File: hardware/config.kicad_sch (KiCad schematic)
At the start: 40 parts, among them J4 JTAG, SW1 219-2MST, U4 GateMate-CCGM1A1, U6 74LVC1G04GM,115, U7 74LVC2G00HK3-7, U8 74LVC2G00HK3-7, U9 AT25QL321-MBUE-T

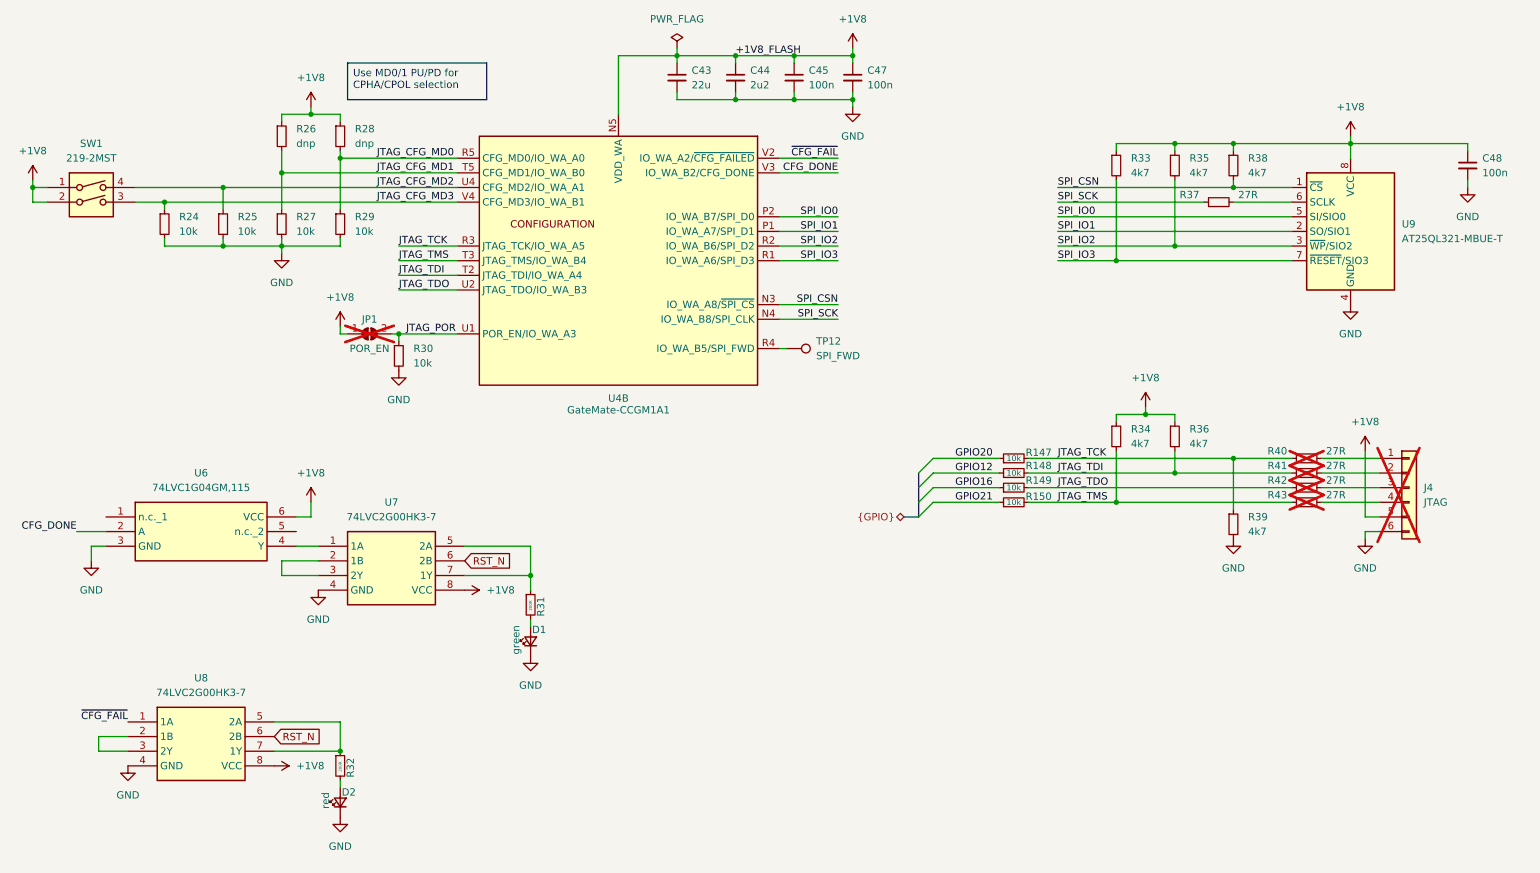
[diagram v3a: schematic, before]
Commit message: big oopsie: change to 4 layer pcb, needs full revision
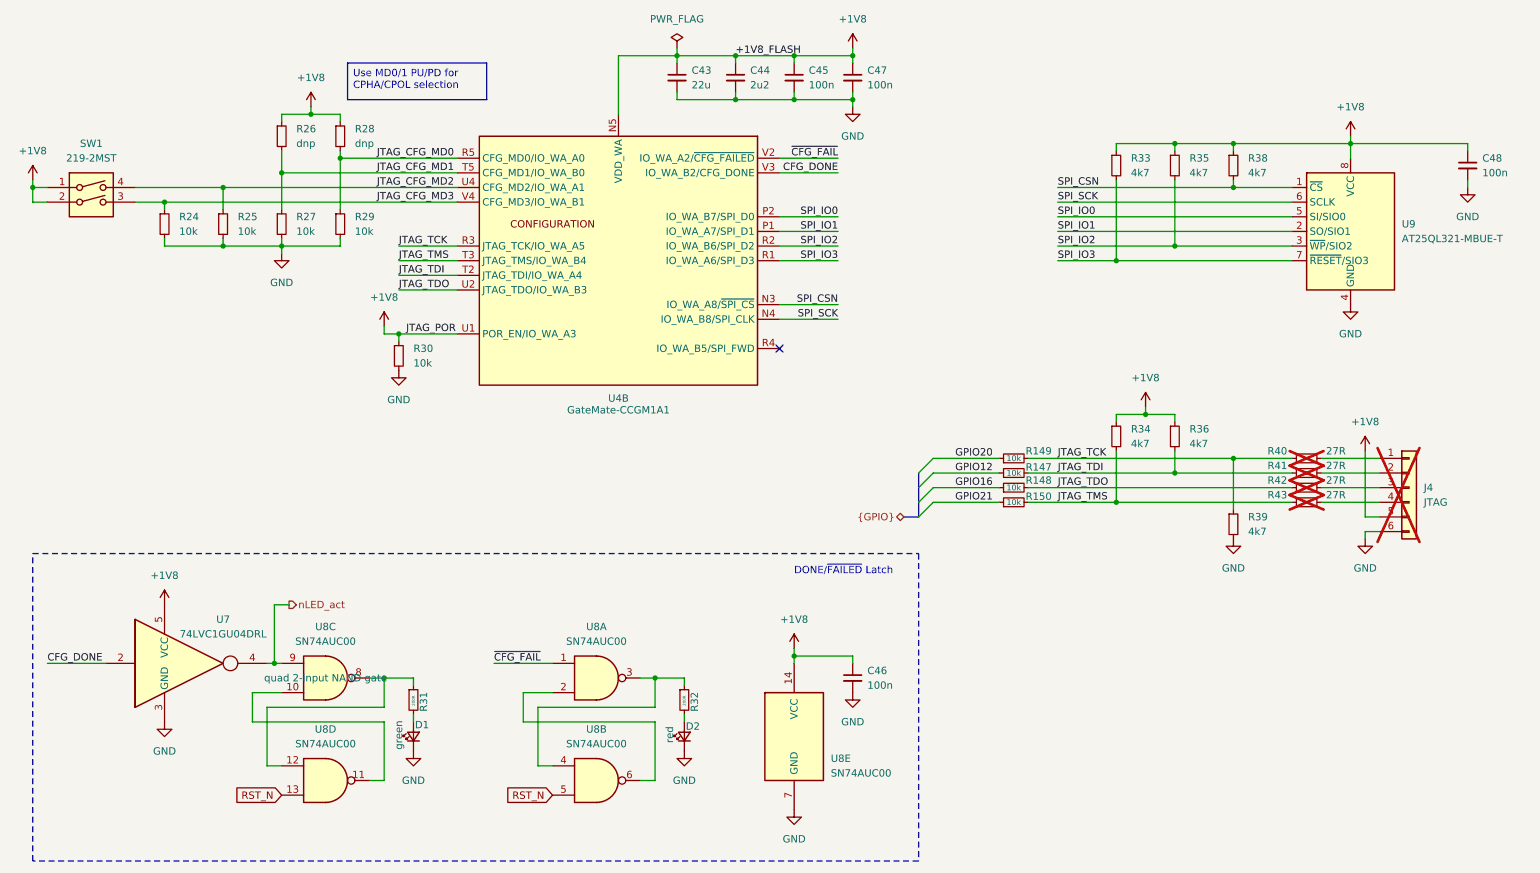
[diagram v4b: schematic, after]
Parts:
- removed JP1: POR_EN, Jumper:SolderJumper-2_P1.3mm_Open_RoundedPad1.0x1.5mm, symbol Jumper:SolderJumper_2_Open
- removed R37: 27R, Resistor_SMD:R_0402_1005Metric, symbol Device:R_Small
- removed TP12: SPI_FWD, TestPoint:TestPoint_Pad_1.0x1.0mm, symbol Connector:TestPoint
- removed U6: 74LVC1G04GM,115, 74LVC1G04GM,115:PESD3V3L5UF115, symbol 74LVC1G04GM_115:74LVC1G04GM,115
- removed U7, U8: 74LVC2G00HK3-7, 74LVC2G00HK3-7:74LVC2G00HK37, symbol 74LVC2G00HK3-7:74LVC2G00HK3-7
- added C46: 100n, Capacitor_SMD:C_0402_1005Metric, symbol Device:C_Small
- added U7: 74LVC1GU04DRL, Package_TO_SOT_SMD:SOT-553, symbol 74xGxx:74LVC1GU04DRL
- added U8: SN74AUC00, Package_DFN_QFN:DHVQFN-14-1EP_2.5x3mm_P0.5mm_EP1x1.5mm, symbol 74xx:74HC00
- D1, D2: footprint Diode_SMD:D_0402_1005Metric -> Diode_SMD:D_0603_1608Metric
- U9: footprint ulx5m-gs:SON80P400X300X60-10N -> Package_SO:SOIC-8_3.9x4.9mm_P1.27mm
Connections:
- net JTAG_POR is gone; now on net +1V8: R30.1, U4.U1 (POR_EN/IO_WA_A3)
- net +1V8: now also C46.1, U7.5 (VCC), U8.14 (VCC)
- net CFG_DONE: now also U7.2
- net GND: now also C46.2, U7.3 (GND), U8.7 (GND)
- net GPIO12: now also R147.1; no longer R148.1
- net GPIO16: now also R148.1; no longer R149.1
- net GPIO20: now also R149.1; no longer R147.1
- net JTAG_TCK: now also R149.2; no longer R147.2
- net JTAG_TDI: now also R147.2; no longer R148.2
- net JTAG_TDO: now also R148.2; no longer R149.2
- net RST_N: now also U8.13, U8.5
- net SPI_SCK: now also U9.6 (SCLK)
- net ~{CFG_FAIL}: now also U8.1
- net at R31.1: now also U8.12, U8.8
- net at R32.1: now also U8.3, U8.4
- new net: U8.10, U8.11
- new net: U8.2, U8.6
- new net nLED_act: U7.4, U8.9
- no-connect marks 0 -> 1
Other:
- note added: "DONE/~{FAILED} Latch"
- moved on the sheet: D1, D2, R147, R148, R149, R31, R32
